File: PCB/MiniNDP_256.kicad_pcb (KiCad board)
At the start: 2 copper layers, 60 x 34 mm, 25 parts, among them J1 Conn_02x20_Odd_Even, M1 MountHole_M2.5, M2 MountHole_M2.5, M3 MountHole_M2.5, M4 MountHole_M2.5, U1 74161, U2 74161, U3 74161, U4 74138, U5 74374, U6 AS6C2008A, U7 741G32

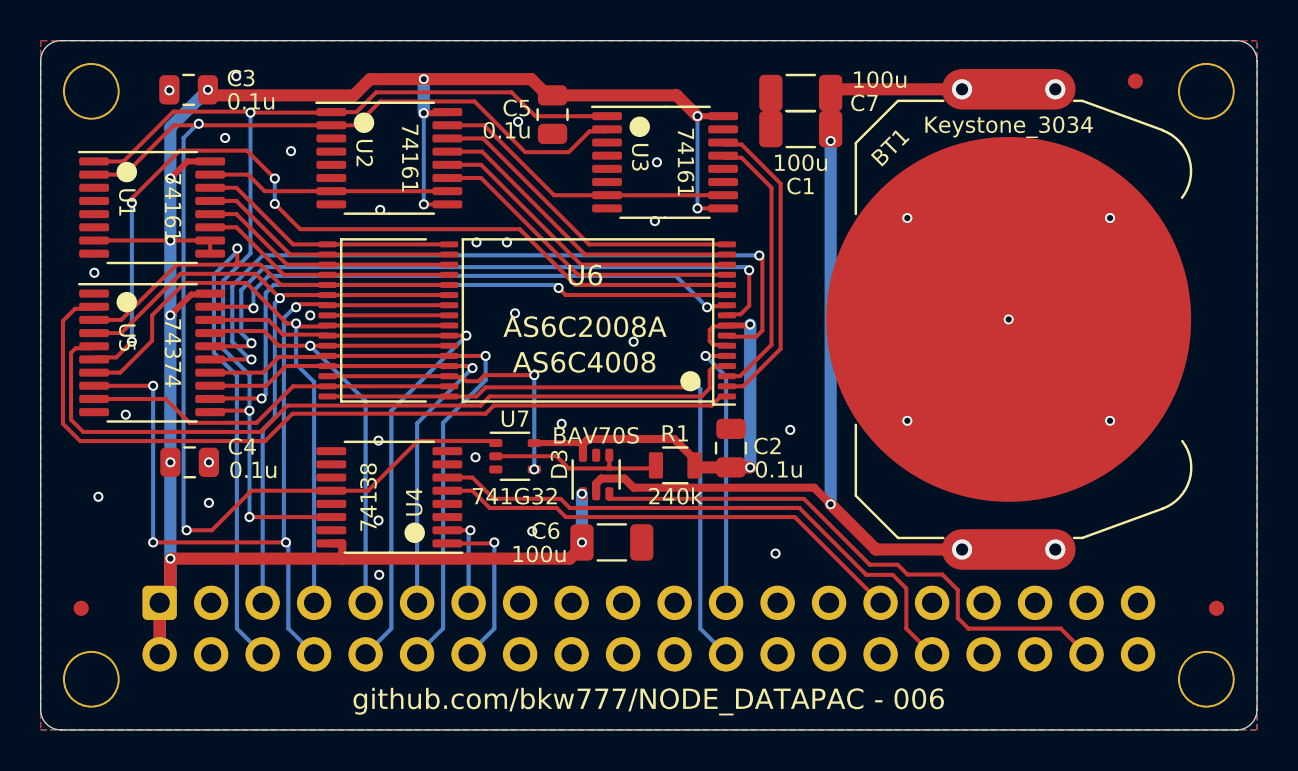
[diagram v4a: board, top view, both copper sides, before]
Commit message: minindp low reverse leakage diode to protect batt
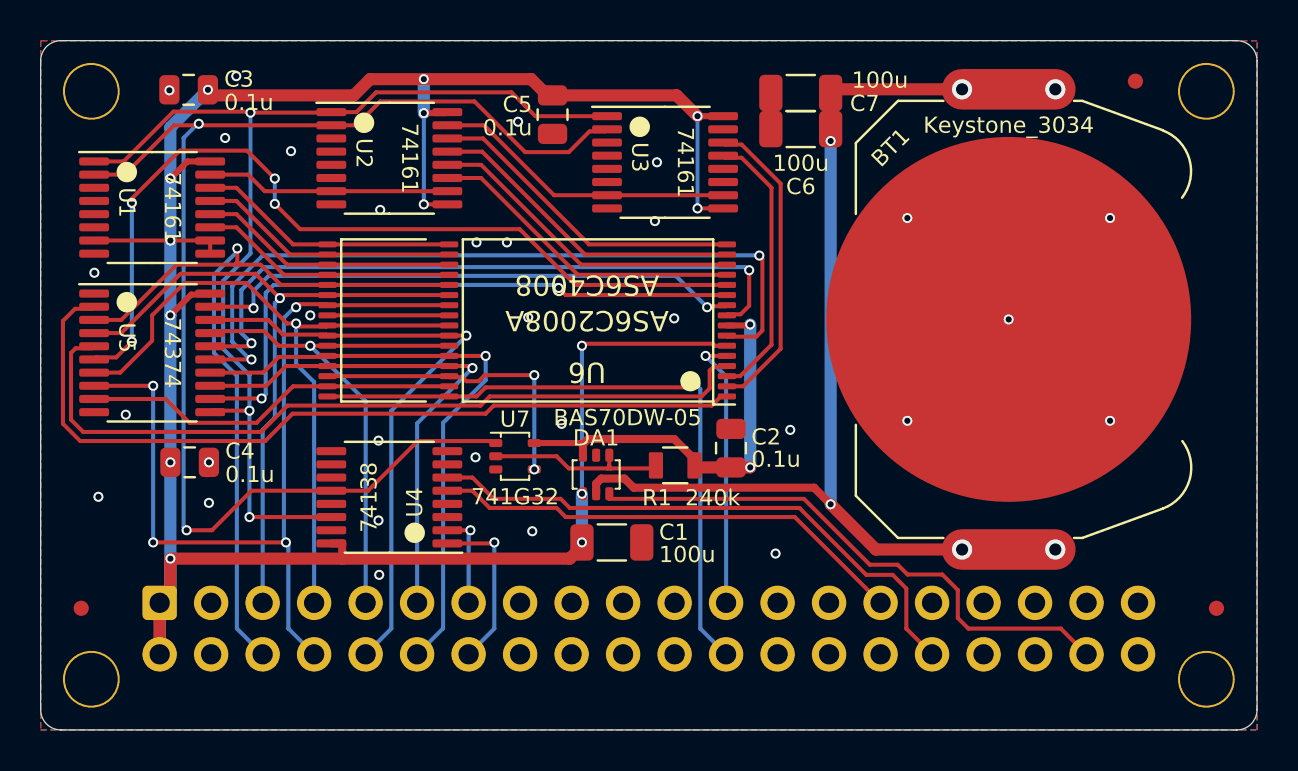
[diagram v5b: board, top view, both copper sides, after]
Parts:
- DA1: renamed from D3; value BAV70S -> BAS70DW-05; footprint 000_LOCAL:SOT-363_SC-70-6 -> 000_LOCAL:SOT-363_SC-70-6_symmetric
- renumbered C6 to C1, C1 to C6
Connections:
- M1 pad : (no net) -> GND
- M2 pad : (no net) -> GND
- M3 pad : (no net) -> GND
- M4 pad : (no net) -> GND
- U6 pad 6: VMEM -> VBUS
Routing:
- net VBUS: track 110.3 -> 124.9 mm, vias 13 -> 14
- net VMEM: track 22.7 -> 20.3 mm

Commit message: caps
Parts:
- removed the C1 at (150.1, 110.8)
- removed the C6 at (159.4, 90.4)
- removed C7: 100u, 000_LOCAL:C_1206
- added C2: 220u, 000_LOCAL:CP_EIA-6032-28, F.Cu at (154.5, 110.9)
- added C3: 1u, 000_LOCAL:C_0805, F.Cu at (133.9, 110.4)
- C1: renamed from C2; value 0.1u -> 1u
- C4: value 0.1u -> 1u
- C5: renamed from C3; value 0.1u -> 1u
- C6: renamed from C5; value 0.1u -> 1u
- moved R1 0.76 mm to (152.5, 106.8)
- moved C1 0.53 mm to (156.5, 106.0)
- moved C6 0.27 mm to (146.9, 89.7)
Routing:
- net VMEM: track 20.3 -> 24.1 mm, vias 2 -> 3
- net /AD2: track 42.8 -> 44.3 mm
- net /~{BYTE}: track 66.0 -> 64.6 mm
- net /BATT+: track 51.5 -> 50.5 mm
- net /SLEEP: track 9.00 -> 8.13 mm
- net GND: vias 31 -> 45

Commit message: teardrops
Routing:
- net GND: vias 45 -> 46

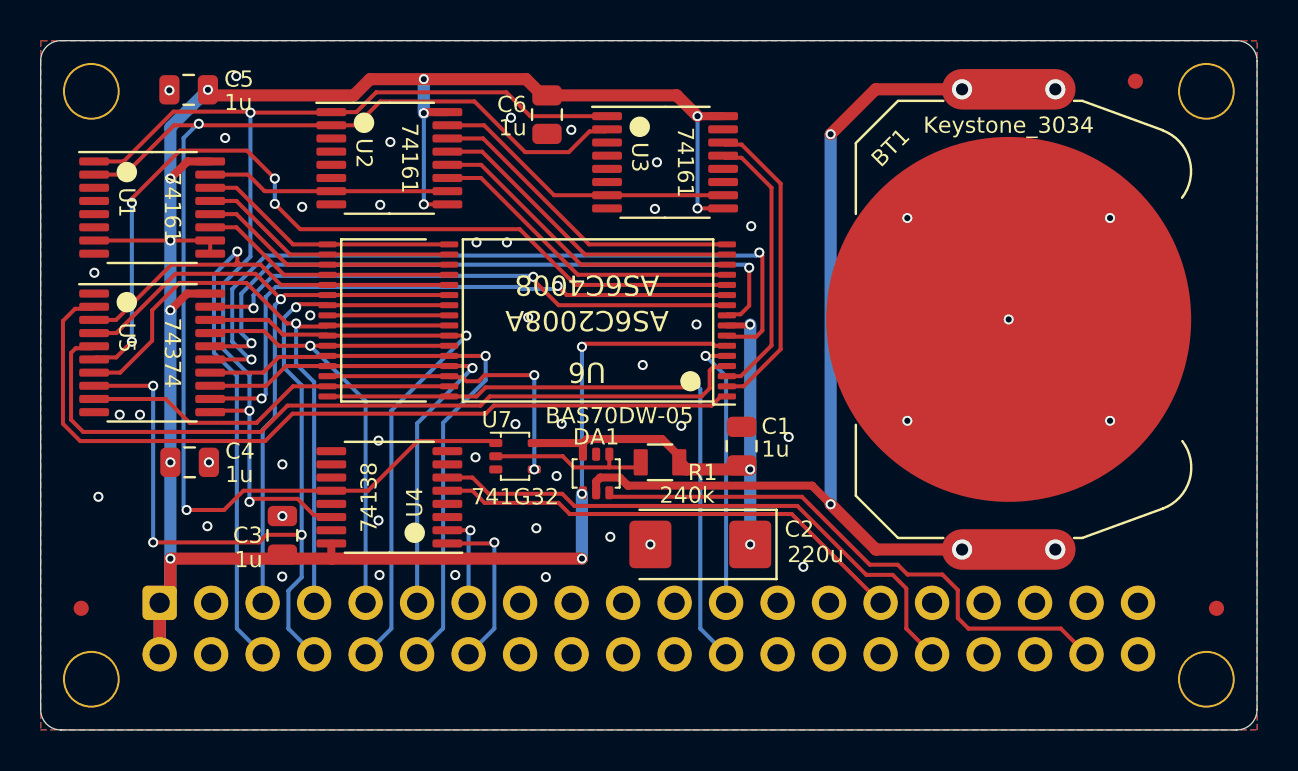
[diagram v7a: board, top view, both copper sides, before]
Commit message: add current limit resistor to C2 cap
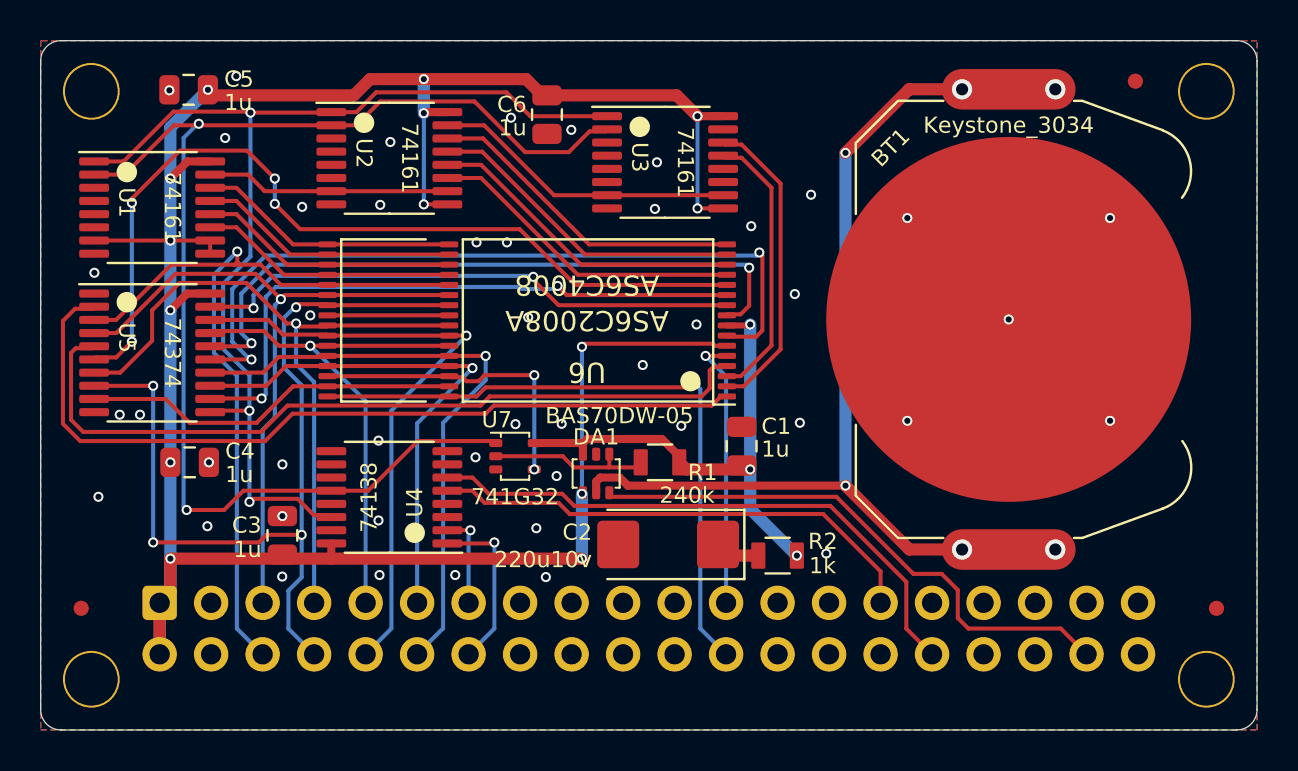
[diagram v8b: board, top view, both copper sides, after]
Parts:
- added R2: 1k, 000_LOCAL:R_0805, F.Cu at (158.3, 111.4)
- C2: value 220u -> 220u10v; footprint 000_LOCAL:CP_EIA-6032-28 -> 000_LOCAL:CP_6032
- moved C2 1.59 mm to (152.9, 110.9)
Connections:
- C2 pad 1: VMEM -> Net-(C2-Pad1)
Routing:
- net Net-(C2-Pad1): track 0.00 -> 2.22 mm
- net /BATT+: track 50.5 -> 48.3 mm
- net VMEM: track 24.1 -> 25.6 mm
- net /Y0: track 23.7 -> 24.6 mm
